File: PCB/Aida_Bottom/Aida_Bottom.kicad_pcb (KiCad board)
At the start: 2 copper layers, 119.7 x 83.3 mm, 15 parts

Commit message: 原点ガイドを追加。基板Mid_InsideのLED穴形状調整
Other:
- board text added: "Center Origin"
- board text added: "Grid Origin"
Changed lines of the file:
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@@
 		(layer "Edge.Cuts")
+	)
+	(gr_line
+		(start 152.4 21.43125)
+		(end 152.4 26.19375)
+		(stroke
+			(width 0.1)
+			(type default)
+		)
+		(layer "User.1")
+	)
+	(gr_circle
+		(center 23.8125 23.8125)
+		(end 25.003125 23.8125)
+		(stroke
+			(width 0.1)
+			(type default)
+		)
+		(fill no)
+		(layer "User.1")
+	)
+	(gr_line
+		(start 21.43125 23.8125)
+		(end 26.19375 23.8125)
+		(stroke
+			(width 0.1)
+			(type default)
+		)
+		(layer "User.1")
+	)
+	(gr_line
+		(start 150.01875 23.8125)
+		(end 154.78125 23.8125)
+		(stroke
+			(width 0.1)
+			(type default)
+		)
+		(layer "User.1")
+	)
+	(gr_circle
+		(center 152.4 23.8125)
+		(end 153.590625 23.8125)
+		(stroke
+			(width 0.1)
+			(type default)
+		)
+		(fill no)
+		(layer "User.1")
+	)
+	(gr_line
+		(start 23.8125 21.43125)
+		(end 23.8125 26.19375)
+		(stroke
+			(width 0.1)
+			(type default)
+		)
+		(layer "User.1")
 	)
 	(gr_text "Top PCB outline"
@@
 		(at 42.267197 32.1469 0)
 		(layer "Eco2.User")
+		(effects
+			(font
+				(size 1 1)
+				(thickness 0.15)
+			)
+			(justify left bottom)
+		)
+	)
+	(gr_text "Grid Origin"
+		(at 20.240625 21.43125 0)
+		(layer "User.1")
+		(effects
+			(font
+				(size 1 1)
+				(thickness 0.15)
+			)
+			(justify left bottom)
+		)
+	)
+	(gr_text "Center Origin"
+		(at 148.828125 21.43125 0)
+		(layer "User.1")
 		(effects
 			(font
@@
 		)
 	)
+	(group ""
+		(members "2126fab4-8ba6-4595-b1c6-7affee21701c" "712a632c-8ac0-4cf6-bf20-8ffc562fab71"
+			"79291d5f-fc49-4cb5-99a0-ab4cadcc6caf" "cd7180aa-16e0-47b7-8b7d-0f9c0b052424"
+		)
+	)
+	(group ""
+		(members "0189092c-aa6e-427e-b8f8-eb8de9e90067" "5c6664ed-3f21-43dd-ac96-83ecd1326359"
+			"c8b3437f-6dd2-40aa-8b77-39a61b41b4ec" "c94bda68-f20d-4da9-b4ec-07049c7b169d"
+		)
+	)

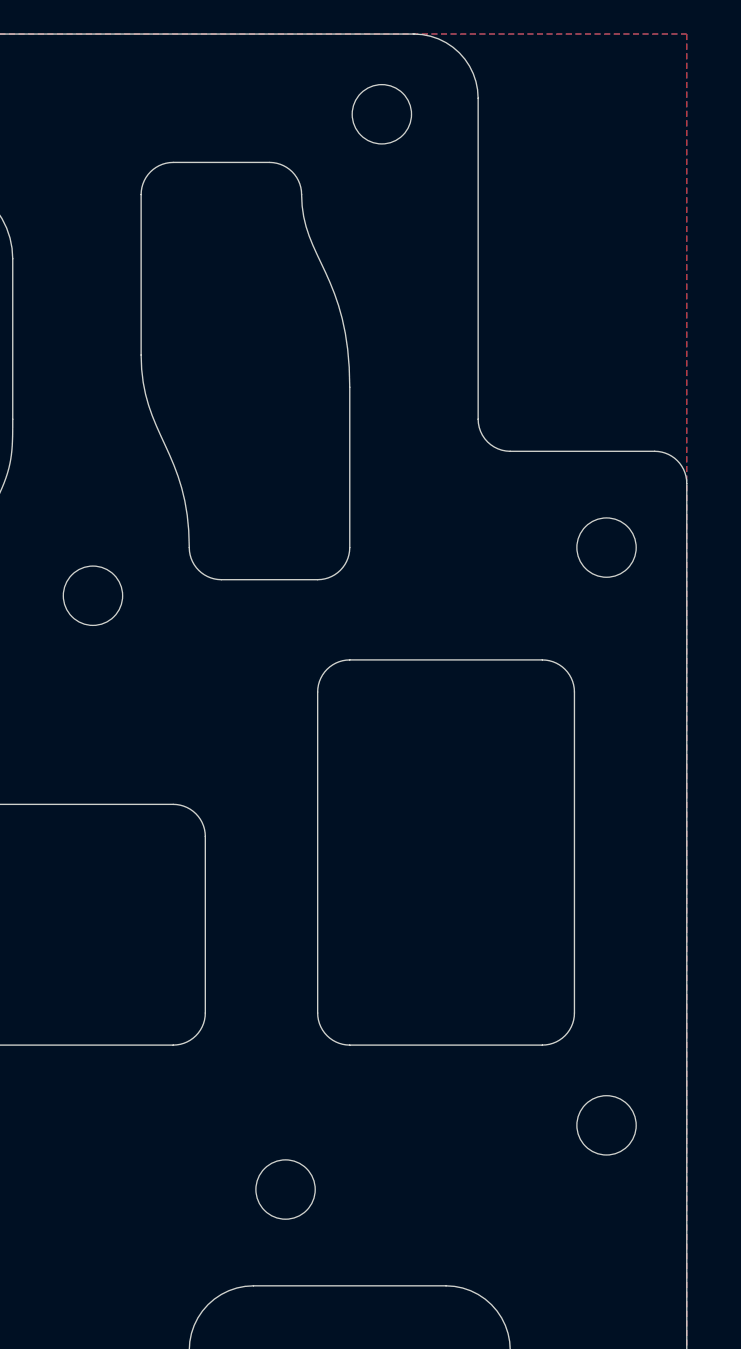
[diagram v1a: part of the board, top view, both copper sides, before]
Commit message: LEDを1/16u下へ移動。 右手のフラッシュメモリとの干渉回避のためボトムプレートの穴位置調整。
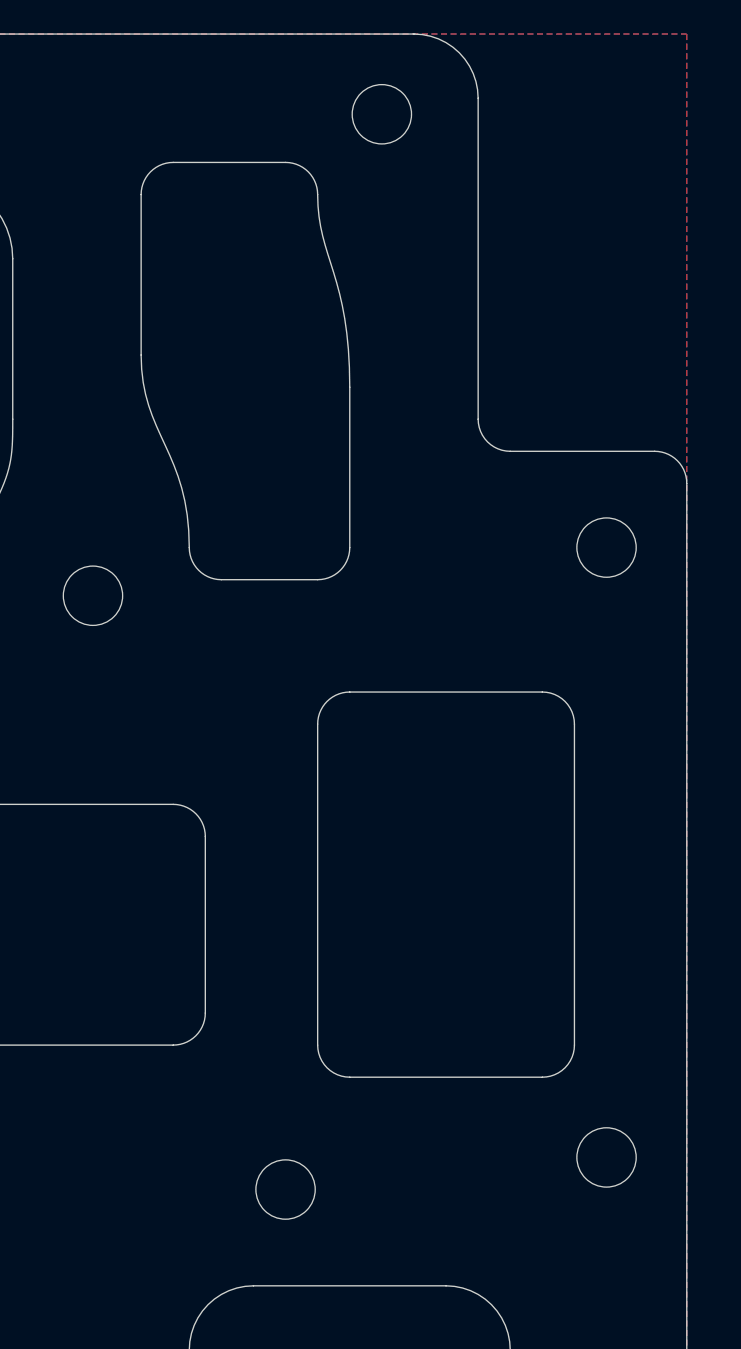
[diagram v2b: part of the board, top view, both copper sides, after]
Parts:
- moved ? 1.19 mm to (147.6, 75.0)
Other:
- outline, holes or cut-outs redrawn
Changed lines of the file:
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@@
 	(footprint ""
 		(layer "F.Cu")
-		(at 147.637604 73.818792)
+		(at 147.637604 75.009375)
 		(property "Reference" ""
 			(at 0 0 0)
@@
 	)
 	(gr_line
-		(start 138.1126 70.842227)
-		(end 145.25635 70.842227)
+		(start 138.1126 72.032859)
+		(end 145.25635 72.032859)
 		(stroke
 			(width 0.05)
@@
 	)
 	(gr_arc
-		(start 146.446978 69.651601)
-		(mid 146.098251 70.493501)
-		(end 145.25635 70.842227)
+		(start 146.446978 70.842233)
+		(mid 146.098248 71.684116)
+		(end 145.25635 72.032859)
 		(stroke
 			(width 0.05)
@@
 	)
 	(gr_arc
-		(start 135.136031 38.100012)
-		(mid 135.977957 38.448773)
-		(end 136.326667 39.29072)
+		(start 135.731344 38.100012)
+		(mid 136.57327 38.448773)
+		(end 136.92198 39.29072)
 		(stroke
 			(width 0.05)
@@
 	(gr_curve
 		(pts
-			(xy 138.112602 46.439331) (xy 138.112596 42.267203) (xy 136.326669 41.671972) (xy 136.326667 39.29072)
+			(xy 138.112602 46.439331) (xy 138.112596 42.267203) (xy 136.92197 41.671972) (xy 136.92198 39.29072)
 		)
 		(stroke
@@
 	)
 	(gr_line
-		(start 145.256346 56.554709)
-		(end 138.112592 56.554709)
+		(start 145.256346 57.745341)
+		(end 138.112592 57.745341)
 		(stroke
 			(width 0.05)
@@
 	)
 	(gr_line
-		(start 136.921964 57.745335)
-		(end 136.921964 69.651595)
+		(start 136.921964 58.935967)
+		(end 136.921964 70.842227)
 		(stroke
 			(width 0.05)
@@
 	)
 	(gr_arc
-		(start 138.112596 70.842227)
-		(mid 137.270692 70.493499)
-		(end 136.921964 69.651595)
+		(start 138.112596 72.032859)
+		(mid 137.270696 71.684129)
+		(end 136.921964 70.842227)
 		(stroke
 			(width 0.05)
@@
 	)
 	(gr_line
-		(start 146.446978 69.651601)
-		(end 146.446978 57.745341)
+		(start 146.446978 70.842233)
+		(end 146.446978 58.935973)
 		(stroke
 			(width 0.05)
@@
 	(gr_line
 		(start 131.564153 38.100012)
-		(end 135.136031 38.100012)
-		(stroke
-			(width 0.05)
-			(type default)
-		)
-		(layer "Edge.Cuts")
-	)
-	(gr_arc
-		(start 145.256346 56.554709)
-		(mid 146.09825 56.903437)
-		(end 146.446978 57.745341)
+		(end 135.731344 38.100012)
+		(stroke
+			(width 0.05)
+			(type default)
+		)
+		(layer "Edge.Cuts")
+	)
+	(gr_arc
+		(start 145.256346 57.745341)
+		(mid 146.098206 58.094088)
+		(end 146.446978 58.935973)
 		(stroke
 			(width 0.05)
@@
 	)
 	(gr_arc
-		(start 136.921964 57.745335)
-		(mid 137.270691 56.903435)
-		(end 138.112592 56.554709)
-		(stroke
-			(width 0.05)
+		(start 136.921964 58.935967)
+		(mid 137.270678 58.09404)
+		(end 138.112592 57.745341)
+		(stroke
+			(width 0.05)
